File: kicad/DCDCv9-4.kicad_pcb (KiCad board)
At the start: 4 copper layers, 85.6 x 54 mm, 216 parts, among them J1 43650-0315, J2 Conn_01x02_Male, J3 Conn_01x02, J4 Conn_01x02_Male, J5 XT60 Male, J6 Conn_01x02_Male, J7 Conn_01x02_Male, J8 Conn_01x02_Male, Q1 PMV20ENR, Q10 IMBG65R050M2HXTMA1, Q11 IMBG65R050M2HXTMA1, Q2 PMV20ENR, Q3 SIHP24N80AE-GE3, Q4 IXYP8N90C3, Q5 PMV20ENR, Q6 PMV20ENR, Q7 PMV20ENR, Q8 ISC015N06NM5LF2ATMA1, Q9 ISC015N06NM5LF2ATMA1, T1 DIY Transformer ETD 39, U1 RP-1212S, U10 LM2904BIDDFR, U11 2EDR8259XXUMA1, U12 UCC25600, U13 ZXRE330ASA-7, U14 LM2904BIDDFR, U2 RT9058-90GVL, U3 MP4541_SOP8-EP, U4 TLV61048DBVR, U5 NCP4305DMTTWG, U6 LM2904BIDDFR, U7 TL431BCDBZR, U8 NCP4305DMTTWG, U9 ACPL-217-50AE

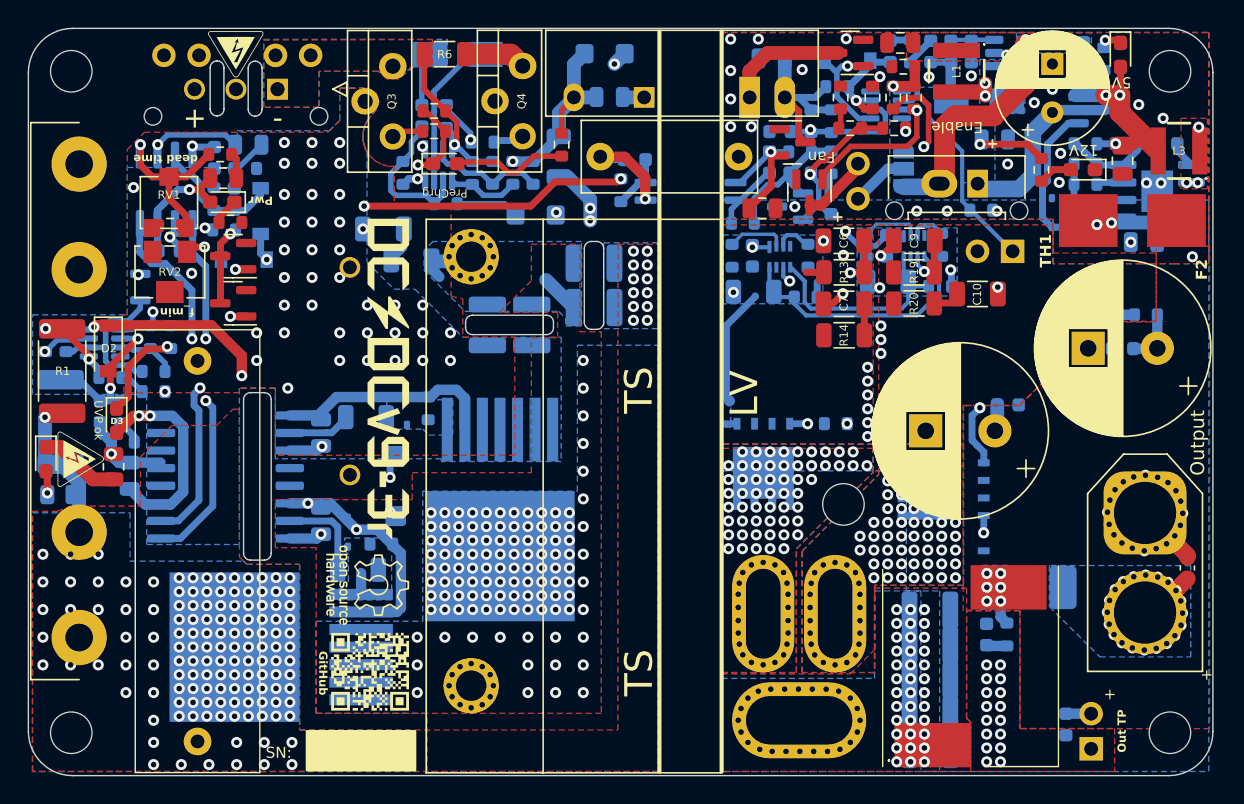
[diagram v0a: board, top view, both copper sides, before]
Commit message: Added ferrite bead to U3, enlarged SR FET cooling surface
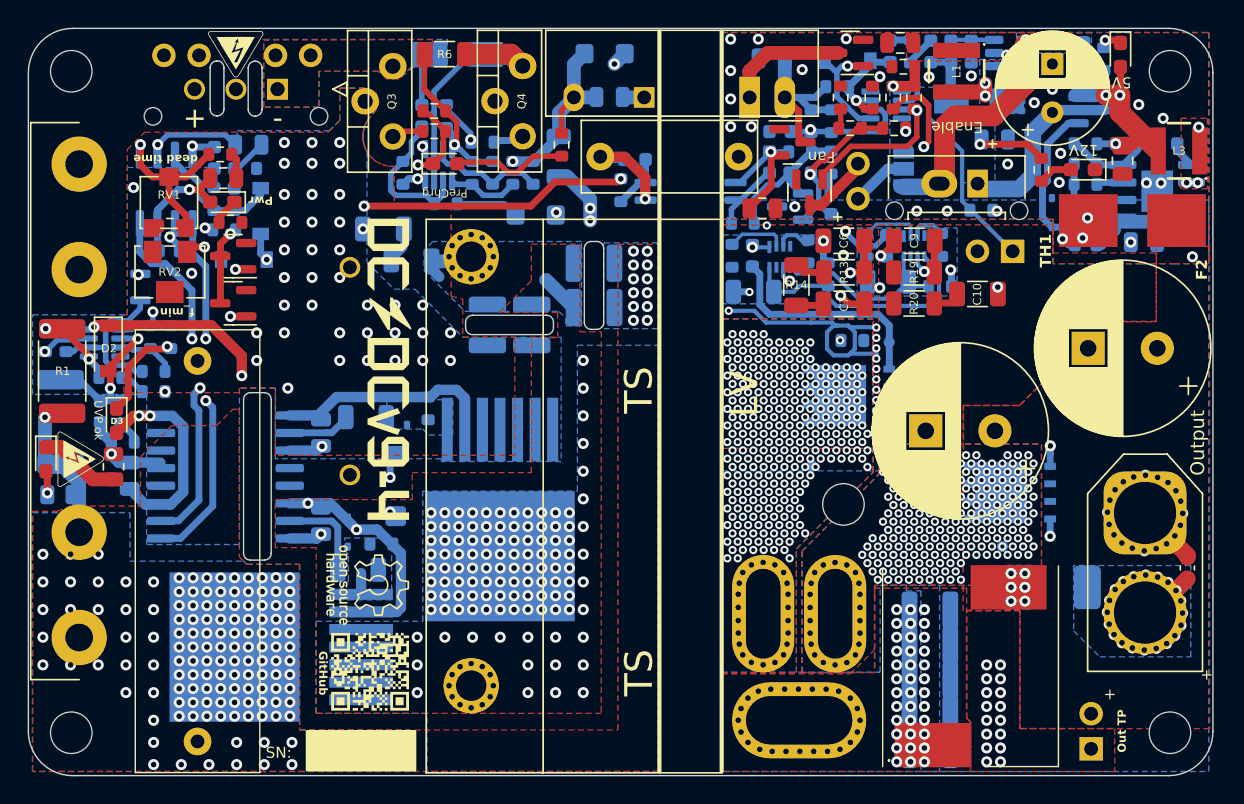
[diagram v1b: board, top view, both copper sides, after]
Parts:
- removed C50, C51, C52, C56, C57: 1nF, DCDC-Footprints:C_0603_1608Metric
- removed R73, R74: 10, DCDC-Footprints:R_0603_1608Metric
- removed TP8: GaN GND2, DCDC-Footprints:TestPoint_Pad_D0.8mm_DC-DC
- added FB1: 470 Ohm, Inductor_SMD:L_0603_1608Metric, B.Cu at (176.4, 90.7)
- D15, D16, D8: value CDSOD323-T12 -> CDSOD323-T15
- Q10, Q11: value IMBG65R050M2HXTMA1 -> IMBG120R026M2HXTMA1
- U1: value RP-1212S -> RP-1215S
- moved NT2 12.4 mm to (162.2, 99.1), turned to -90 degrees
- moved TP6 12.3 mm to (162.2, 97.7)
- moved Q9 7.92 mm to (159.3, 101.5), turned to -90 degrees
- moved TH2 6.13 mm to (159.5, 97.6), turned to 0 degrees
- moved TP4 6.02 mm to (162.2, 104.8)
- moved TP1 5.79 mm to (173.8, 105.2)
- moved R14 5.01 mm to (155.5, 93.6), turned to -90 degrees
- moved TP2 4.81 mm to (173.8, 111.7)
- moved NT1 4.81 mm to (173.8, 106.3)
- moved Q8 4.81 mm to (170.9, 108.6)
- moved TP3 4.45 mm to (170.4, 112.5)
- moved R40 2.31 mm to (157.8, 92.8), turned to -90 degrees
- moved F3 1.75 mm to (174.0, 115.4)
- moved G*** 0.52 mm to (126.1, 99.6)
- moved R38 0.30 mm to (156.3, 91.1)
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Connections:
- C15 pad 2: +24V -> Net-(U3-EN)
- C53 pad 2: +24V -> Net-(U3-EN)
- U3 pad 1: +24V -> Net-(U3-EN)
- U3 pad 8: +24V -> Net-(U3-EN)
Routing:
- net GND: track 13.2 -> 44.8 mm, vias 78 -> 80
- net Net-(U3-EN): track 0.00 -> 10.4 mm
- net 24V_TP: track 74.5 -> 64.4 mm
- net Net-(U8-GND): track 9.63 -> 16.7 mm
- net +24V: track 9.49 -> 2.76 mm, vias 2 -> 3
- net Net-(Q9-G): track 15.7 -> 21.8 mm
- net Net-(U6A--): track 36.3 -> 32.9 mm
- net Net-(U5-DRV): track 15.9 -> 13.5 mm
- net Net-(U5-GND): track 18.0 -> 20.1 mm
- net Net-(C57-Pad2): track 1.41 -> 0.00 mm
- net Net-(C56-Pad2): track 1.36 -> 0.00 mm
- net /Synchronous Rectification/3: track 1.30 -> 2.22 mm, vias 78 -> 305
- net Net-(Q8-G): track 24.7 -> 25.6 mm
- net Net-(U5-TRIG/DIS): track 18.6 -> 19.1 mm
- net /Synchronous Rectification/5: vias 83 -> 240
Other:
- board text added: "I need a Via, Via, Via is what I need."
- board text removed: "Please do not release the magic smoke. It is necessary for operation."

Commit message: moved testpoint
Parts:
- moved TP5 2.09 mm to (158.4, 105.5)
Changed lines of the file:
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@@
 		(tags "resistor")
 		(property "Reference" "R14"
-			(at -0.015 -0.005 360)
+			(at -0.015 -0.005 0)
 			(layer "F.SilkS")
 			(effects
@@
 		)
 		(property "Value" "470pF"
-			(at 0 1.85 360)
+			(at 0 1.85 0)
 			(layer "F.Fab")
 			(effects
@@
 		)
 		(fp_text user "${REFERENCE}"
-			(at 0 0 360)
+			(at 0 0 0)
 			(layer "F.Fab")
 			(effects
@@
 		(tags "Schottky Diode")
 		(property "Reference" "D14"
-			(at 0 0 270)
+			(at 0 0 -90)
 			(layer "B.SilkS")
 			(effects
@@
 		(tags "inductor")
 		(property "Reference" "FB1"
-			(at 0 1.43 360)
+			(at 0 1.43 0)
 			(layer "B.SilkS")
 			(hide yes)
@@
 		)
 		(property "Value" "470 Ohm"
-			(at 0 -1.43 360)
+			(at 0 -1.43 0)
 			(layer "B.Fab")
 			(effects
@@
 		)
 		(fp_text user "${REFERENCE}"
-			(at 0 0 360)
+			(at 0 0 0)
 			(layer "B.Fab")
 			(effects
@@
 	(footprint "DCDC-Footprints:TestPoint_Pad_D0.8mm_DC-DC"
 		(layer "B.Cu")
-		(at 156.595 106.6 180)
+		(at 158.375 105.5 180)
 		(descr "SMD pad as test Point, diameter 1.0mm")
 		(tags "test point SMD pad")

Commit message: added PCBA BOM, added lots of JLC part numbers
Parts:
- R56, R58: value 10 -> 4.7
